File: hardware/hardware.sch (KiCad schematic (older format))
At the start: 103 parts, among them J1 DB25_Female, J2 USB_B_Micro, J3 RJ45_Bel_SI-60062-F-68net, J4 Conn_01x02_Male, J5 Conn_01x02_Male, U1 MIC5319, U11 ENC28J60x-SO, U12 74LVC14, U2 74LVTH126, U3 74LVTH126, U4 LM1117-ADJ, U5 74LVTH126, U6 74LVTH126, U7 STM32F072R8Tx, U8 74LVC245, Y1 8MHz, Y2 25MHz

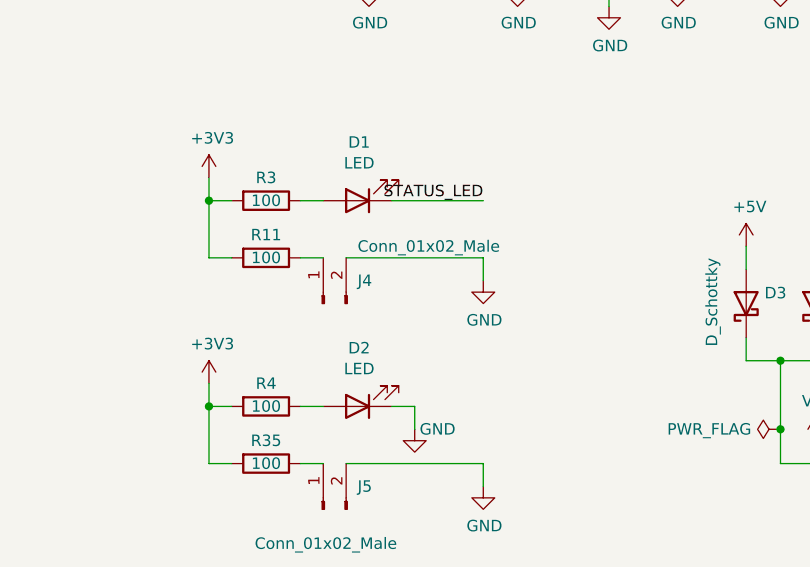
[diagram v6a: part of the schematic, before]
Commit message: fix: wrong pins on LEDs connectors
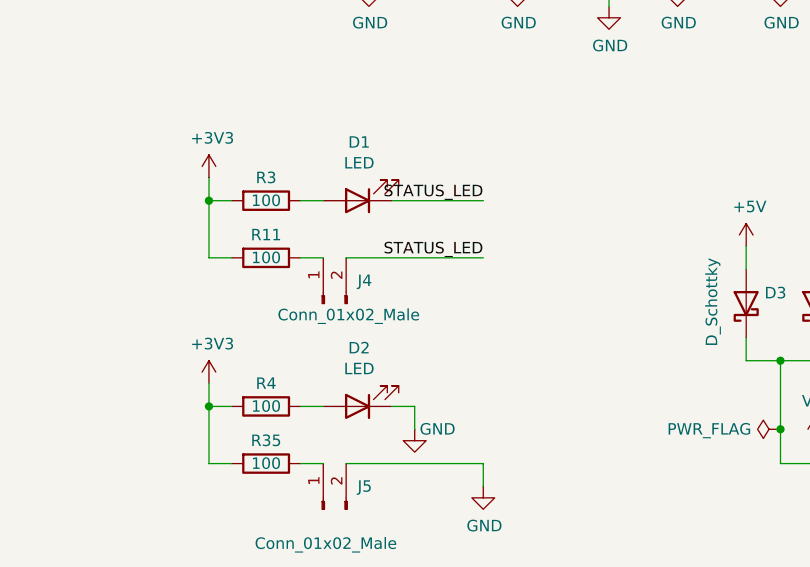
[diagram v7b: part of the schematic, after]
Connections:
- net GND: no longer J4.2 (Pin_2)
- net STATUS_LED: now also J4.2 (Pin_2)
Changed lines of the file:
@@
 P 1500 10000
 F 0 "J4" V 1600 9850 50  0000 R CNN
-F 1 "Conn_01x02_Male" V 1750 9850 50  0000 R CNN
+F 1 "Conn_01x02_Male" V 1450 10200 50  0000 R CNN
 F 2 "Connector_PinHeader_2.54mm:PinHeader_1x02_P2.54mm_Vertical" H 1500 10000 50  0001 C CNN
 F 3 "~" H 1500 10000 50  0001 C CNN
 	1    1500 10000
 	0    -1   -1   0
-$EndComp
-Wire Wire Line
-	1600 9800 2200 9800
-Wire Wire Line
-	2200 9800 2200 9900
-$Comp
-L power:GND #PWR?
-U 1 1 612D7C08
-P 2200 9900
-F 0 "#PWR?" H 2200 9650 50  0001 C CNN
-F 1 "GND" H 2205 9727 50  0000 C CNN
-F 2 "" H 2200 9900 50  0001 C CNN
-F 3 "" H 2200 9900 50  0001 C CNN
-	1    2200 9900
-	1    0    0    -1
 $EndComp
 Wire Wire Line
@@
 Wire Wire Line
 	1800 3200 2150 3200
+Text Label 2200 9800 2    50   ~ 0
+STATUS_LED
+Wire Wire Line
+	1600 9800 2200 9800
 $EndSCHEMATC

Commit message: feat: update BOM
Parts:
- C1, C10, C11, C12, C13, C14, C15, C16, C17, C18, C19, C2, C20, C21, C22, C23, C24, C25, C26, C27, C28, C29, C3, C30, C31, C32, C33, C34, C35, C4, C5, C6, C7, C8, C9, D1, D2, FB1, H1, H2, H3, H4, J2, J3, J4, J5, JP1, R1, R14, R15, R2, RN1, RN2, U11, U12, U2, U3, U4, U5, U6, U7, U8: checked (none) -> ok
- C36: value 0.1uF -> 100nF; Digi-Key_PN CL31B104KBCNNNC -> 1276-1017-1-ND; checked (none) -> ok
- D3, D4: Digi-Key_PN RB521S30T1GOSCT-ND -> NSR0520V2T1GOSCT-ND; checked (none) -> ok
- J1: Digi-Key_PN 609-1507-ND -> 2057-DPD-25-00-B3-ND; checked (none) -> ok
- R10, R36, R7, R9: Digi-Key_PN RMCF0603JT10K0CT-ND -> RMCF0805JT10K0CT-ND; checked (none) -> ok
- R11, R3, R35, R4: Digi-Key_PN RMCF0805FT165RCT-ND -> RMCF0805FT100RCT-ND; checked (none) -> ok
- R12, R13: Digi-Key_PN (none) -> RMCF0805JT10K0CT-ND; checked (none) -> ok
- R16: Digi-Key_PN RNCF0603DTE2K32CT-ND -> RNCF0805DTE2K32CT-ND; checked (none) -> ok
- R17, R18, R19, R20: Digi-Key_PN RNCP0603FTD49R9CT -> RNCF0805DTE2K32CT-ND; checked (none) -> ok
- R21, R22, R23, R24, R25, R26, R27, R28, R29, R30, R31, R32, R33, R34, R8: Digi-Key_PN (none) -> RMCF0805FT3K30CT-ND; checked (none) -> ok
- R5, R6: Digi-Key_PN RMCF0603FT22R0CT-ND -> RMCF0805FT22R0CT-ND; checked (none) -> ok
- S1: Digi-Key_PN TL3301AF160QG -> EG2526CT-ND; checked (none) -> ok
- S2: value PTS645SM43SMTR92_LFS -> SWITCH; Digi-Key_PN TL3301AF160QG -> EG2526CT-ND; checked (none) -> ok
- U1: Digi-Key_PN MIC5319-3.3YD5-TR -> 576-1910-1-ND; checked (none) -> ok
- Y1: Digi-Key_PN 887-1253-ND -> 887-1233-ND; checked (none) -> ok
- Y2: Digi-Key_PN 887-1233-ND -> 887-1253-ND; checked (none) -> ok
